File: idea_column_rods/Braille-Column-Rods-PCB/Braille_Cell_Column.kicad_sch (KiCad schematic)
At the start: 11 parts, among them M1 Stepper_Motor_bipolar, U1 DRV8847SPWR, U17 MT910xET

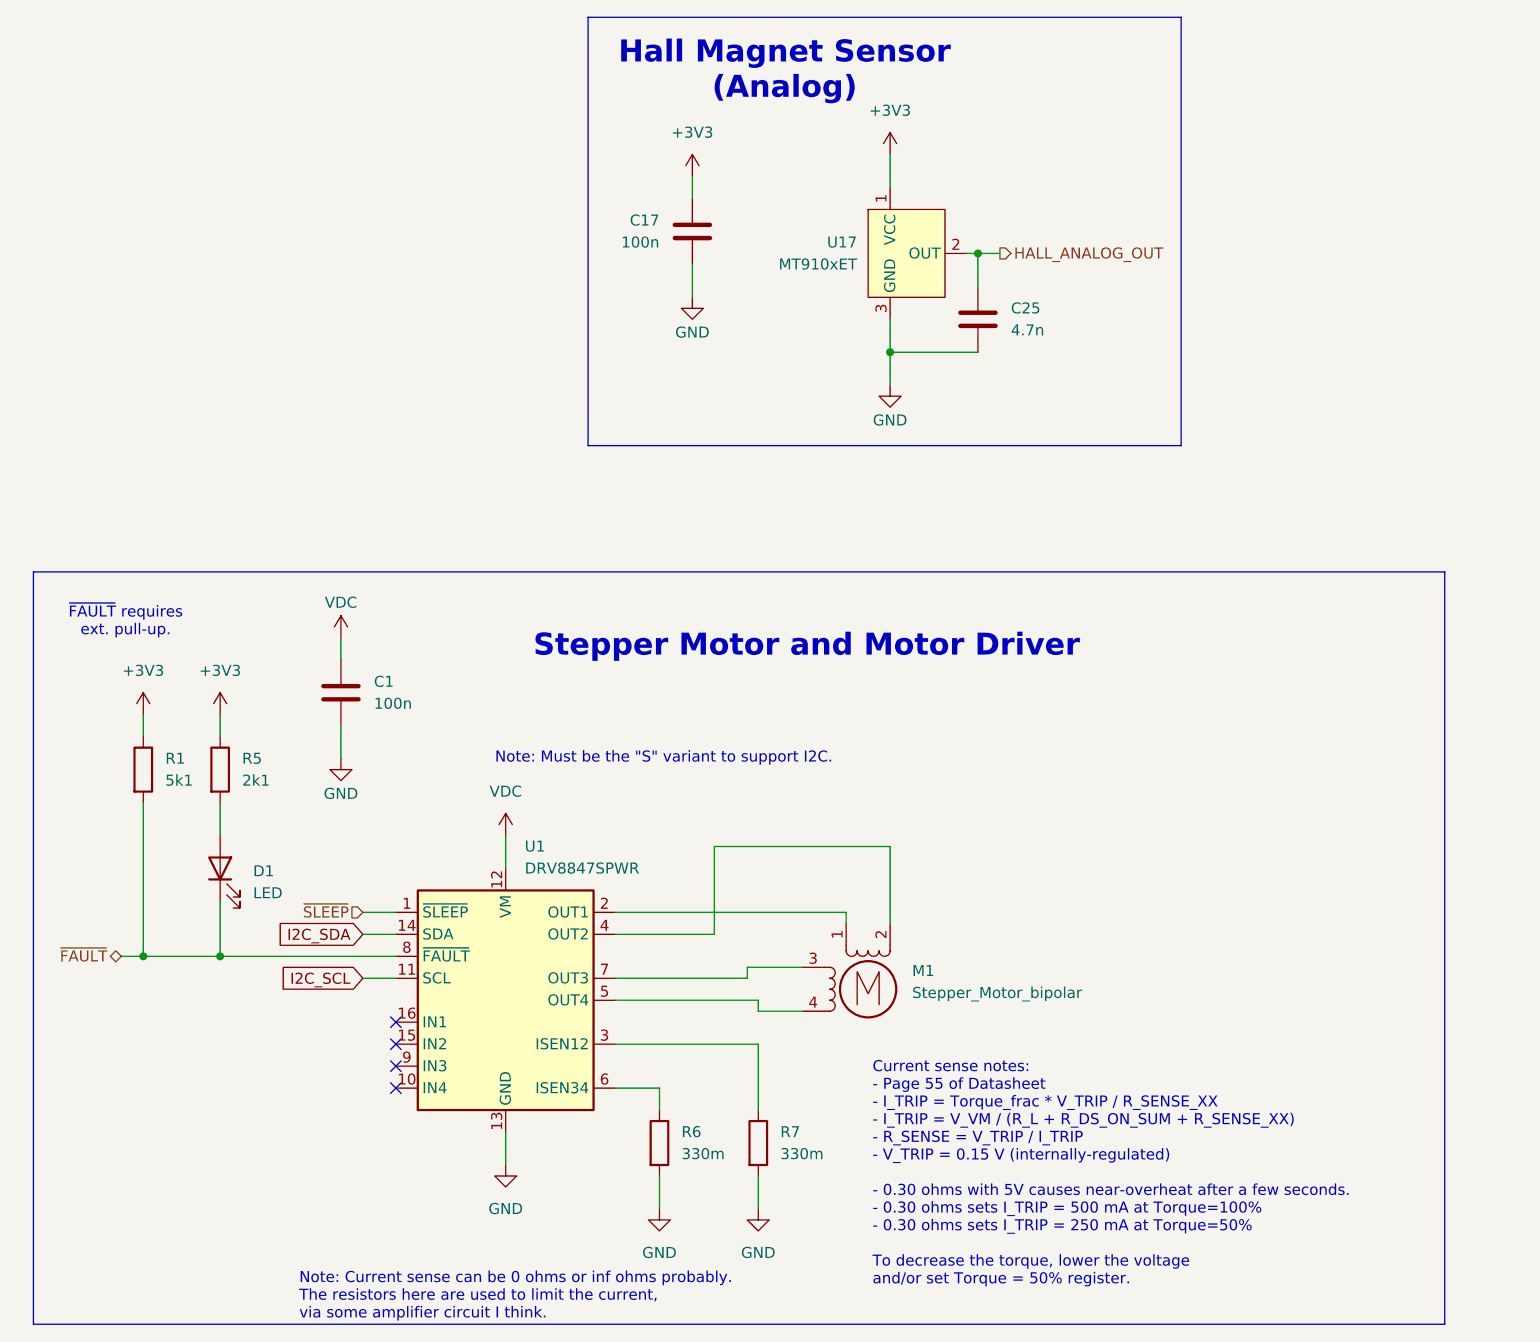
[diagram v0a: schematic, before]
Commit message: Create PCB and CAD for Type 4 Rev 1 rod cams (#13)
* WIP: Rods PCB placement

* WIP: Place the housing and motor X

* WIP: Position everything

* WIP: Update tight placement of DC motor

* WIP: Layout and route the stepper driver

* WIP: Motor layout is good

* WIP: Manual routing and silkscreens

* Comments

* Big routing

* Clean up DRC (mostly footprints)

* Fix spacing issue on top

* Fix spacing issues on bottom

* Create render of 6mm motor, add to PCB

* WIP: Get cams good

* WIP: Reorder the cam bushing and hall sensor

* Finish and tag release

* Complete type 4 rev 1

* Create dc_motor_clamp cad
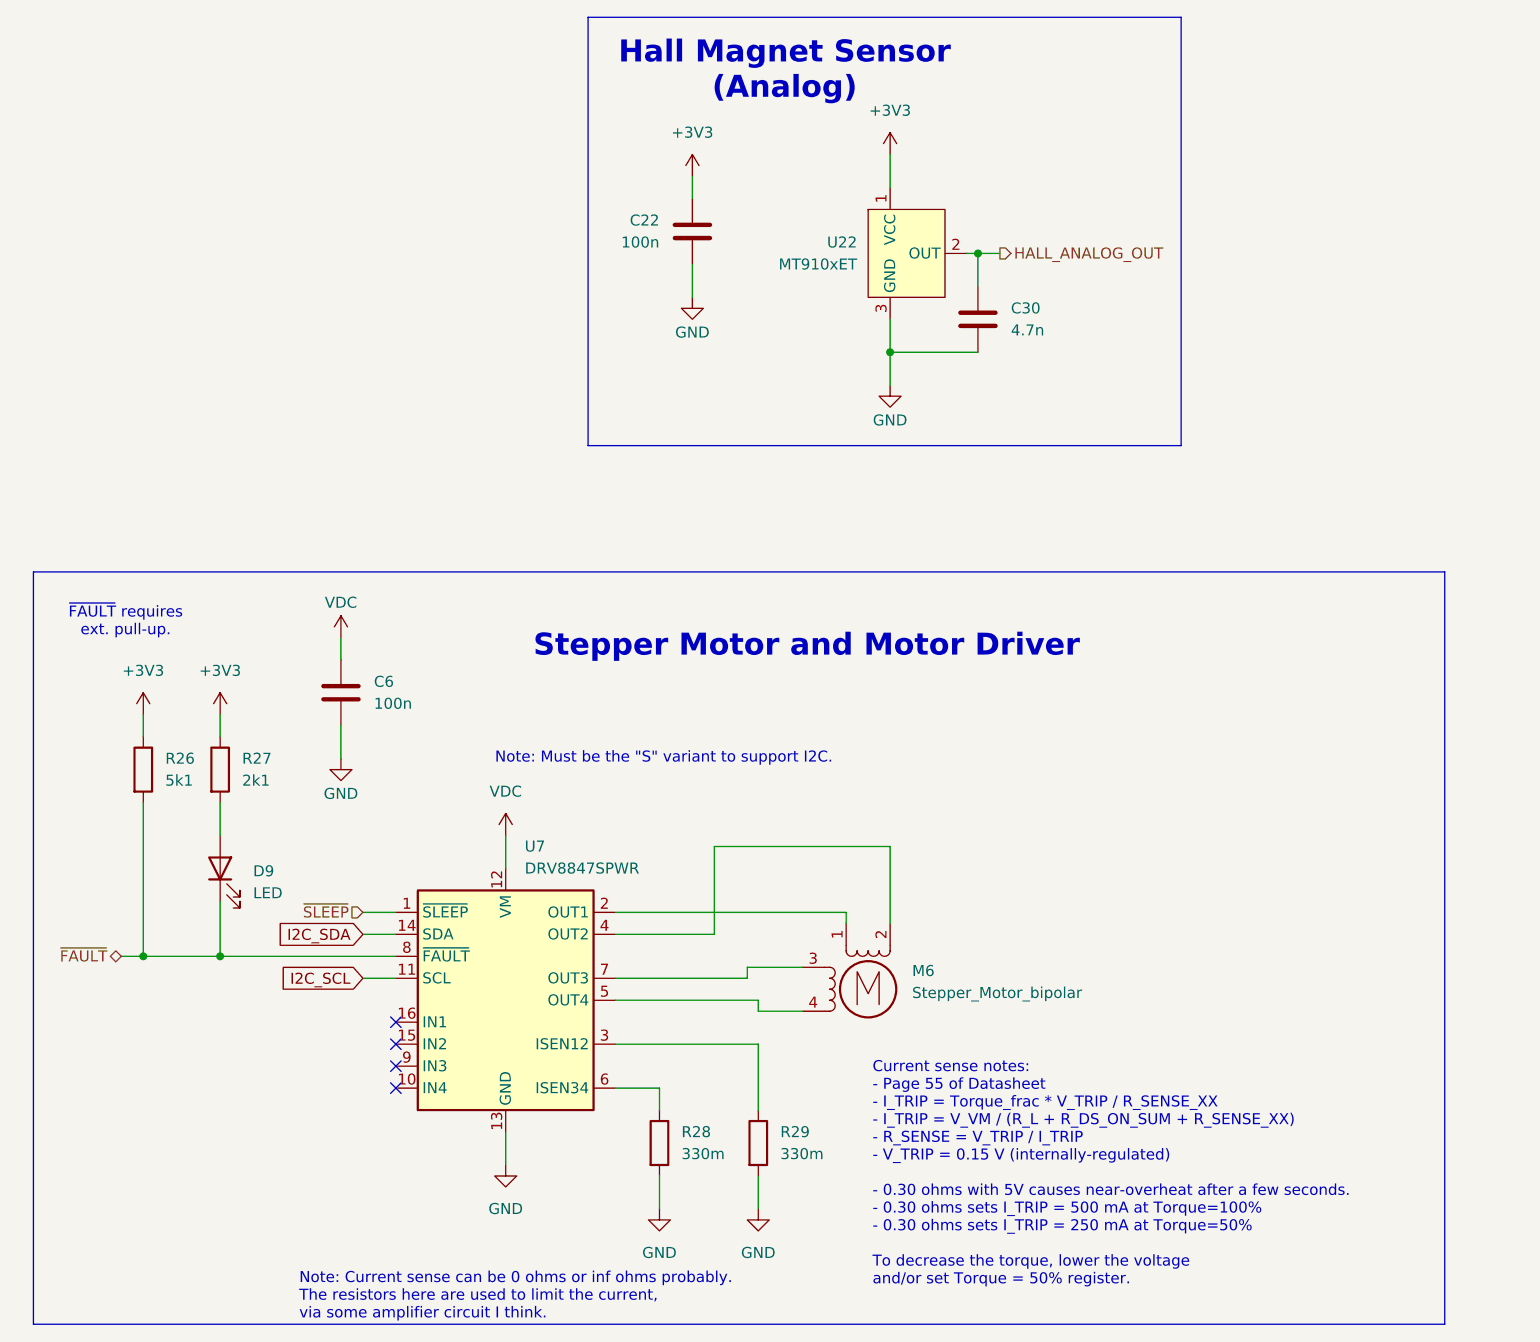
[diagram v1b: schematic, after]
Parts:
- M6: renamed from M1; footprint 00-lib-footprints:MicroStepper_8mm-2mmGear -> 00-lib-footprints:MicroStepper_4.7_OD
- U22: renamed from U17; footprint Package_TO_SOT_SMD:SOT-23 -> 00-lib-footprints:SOT-23-Hall
- renumbered C17 to C22, C25 to C30, C1 to C6, D1 to D9, R1 to R26, R5 to R27, R6 to R28, R7 to R29, U1 to U7
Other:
- title: (none) -> Braille Cam Rod Prototype (Type 4)
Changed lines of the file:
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@@
 	(generator_version "8.0")
 	(paper "USLetter")
+	(title_block
+		(title "Braille Cam Rod Prototype (Type 4)")
+		(date "2025-01-06")
+		(rev "Rev 1")
+	)
 	(junction
 		(at 129.54 53.34)
@@
 		(on_board yes)
 		(dnp no)
-		(property "Reference" "#PWR06"
+		(property "Reference" "#PWR066"
 			(at 66.04 106.68 0)
 			(effects
@@
 		(dnp no)
 		(fields_autoplaced yes)
-		(property "Reference" "R5"
+		(property "Reference" "R27"
 			(at 54.61 100.3299 0)
 			(effects
@@
 		(dnp no)
 		(fields_autoplaced yes)
-		(property "Reference" "D1"
+		(property "Reference" "D9"
 			(at 55.88 113.3474 90)
 			(effects
@@
 		(dnp no)
 		(fields_autoplaced yes)
-		(property "Reference" "M1"
+		(property "Reference" "M6"
 			(at 132.08 124.879 0)
 			(effects
@@
 			)
 		)
-		(property "Footprint" "00-lib-footprints:MicroStepper_8mm-2mmGear"
+		(property "Footprint" "00-lib-footprints:MicroStepper_4.7_OD"
 			(at 127.254 127.254 0)
 			(effects
@@
 		(dnp no)
 		(fields_autoplaced yes)
-		(property "Reference" "#PWR013"
+		(property "Reference" "#PWR068"
 			(at 85.09 153.67 0)
 			(effects
@@
 		(dnp no)
 		(fields_autoplaced yes)
-		(property "Reference" "#PWR03"
+		(property "Reference" "#PWR063"
 			(at 43.18 99.06 0)
 			(effects
@@
 		(on_board yes)
 		(dnp no)
-		(property "Reference" "#PWR0115"
+		(property "Reference" "#PWR0125"
 			(at 106.68 53.34 0)
 			(effects
@@
 		(dnp no)
 		(fields_autoplaced yes)
-		(property "Reference" "#PWR021"
+		(property "Reference" "#PWR069"
 			(at 102.87 158.75 0)
 			(effects
@@
 		(dnp no)
 		(fields_autoplaced yes)
-		(property "Reference" "#PWR0114"
+		(property "Reference" "#PWR0124"
 			(at 106.68 36.83 0)
 			(effects
@@
 		(dnp no)
 		(fields_autoplaced yes)
-		(property "Reference" "R1"
+		(property "Reference" "R26"
 			(at 45.72 100.3299 0)
 			(effects
@@
 		(on_board yes)
 		(dnp no)
-		(property "Reference" "#PWR057"
+		(property "Reference" "#PWR075"
 			(at 66.04 90.17 0)
 			(effects
@@
 		(dnp no)
 		(fields_autoplaced yes)
-		(property "Reference" "R6"
+		(property "Reference" "R28"
 			(at 105.41 143.5099 0)
 			(effects
@@
 		(dnp no)
 		(fields_autoplaced yes)
-		(property "Reference" "C1"
+		(property "Reference" "C6"
 			(at 69.85 91.4399 0)
 			(effects
@@
 		(dnp no)
 		(fields_autoplaced yes)
-		(property "Reference" "C25"
+		(property "Reference" "C30"
 			(at 143.51 48.2599 0)
 			(effects
@@
 		(dnp no)
 		(fields_autoplaced yes)
-		(property "Reference" "U17"
+		(property "Reference" "U22"
 			(at 125.73 40.6399 0)
 			(effects
@@
 			)
 		)
-		(property "Footprint" "Package_TO_SOT_SMD:SOT-23"
+		(property "Footprint" "00-lib-footprints:SOT-23-Hall"
 			(at 125.73 60.198 0)
 			(effects
@@
 		(on_board yes)
 		(dnp no)
-		(property "Reference" "#PWR0138"
+		(property "Reference" "#PWR0143"
 			(at 129.54 63.5 0)
 			(effects
@@
 		(dnp no)
 		(fields_autoplaced yes)
-		(property "Reference" "#PWR04"
+		(property "Reference" "#PWR064"
 			(at 52.07 99.06 0)
 			(effects
@@
 		(on_board yes)
 		(dnp no)
-		(property "Reference" "C17"
+		(property "Reference" "C22"
 			(at 102.87 38.0999 0)
 			(effects
@@
 		(dnp no)
 		(fields_autoplaced yes)
-		(property "Reference" "#PWR0130"
+		(property "Reference" "#PWR0135"
 			(at 129.54 34.29 0)
 			(effects
@@
 		(dnp no)
 		(fields_autoplaced yes)
-		(property "Reference" "#PWR026"
+		(property "Reference" "#PWR070"
 			(at 114.3 158.75 0)
 			(effects
@@
 		(dnp no)
 		(fields_autoplaced yes)
-		(property "Reference" "#PWR05"
+		(property "Reference" "#PWR039"
 			(at 85.09 113.03 0)
 			(effects
@@
 		(dnp no)
 		(fields_autoplaced yes)
-		(property "Reference" "R7"
+		(property "Reference" "R29"
 			(at 116.84 143.5099 0)
 			(effects
@@
 		(dnp no)
 		(fields_autoplaced yes)
-		(property "Reference" "U1"
+		(property "Reference" "U7"
 			(at 87.2841 110.49 0)
 			(effects
